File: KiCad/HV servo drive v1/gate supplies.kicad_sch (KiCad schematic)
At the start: 21 parts, among them U20 WRF0505S-3WR2, U21 B0505MT-1WR4, U8 B0505MT-1WR4

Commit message: KiCad 8.0 update
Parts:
- renumbered C105 to C101, C26 to C103, C44 to C104, C106 to C105, C103 to C106, C42 to C26, C104 to C42, C101 to C43, C43 to C44, L6 to L10, L10 to L6, TP5 to TP3, TP3 to TP5, U21 to U20, U8 to U21, U20 to U8

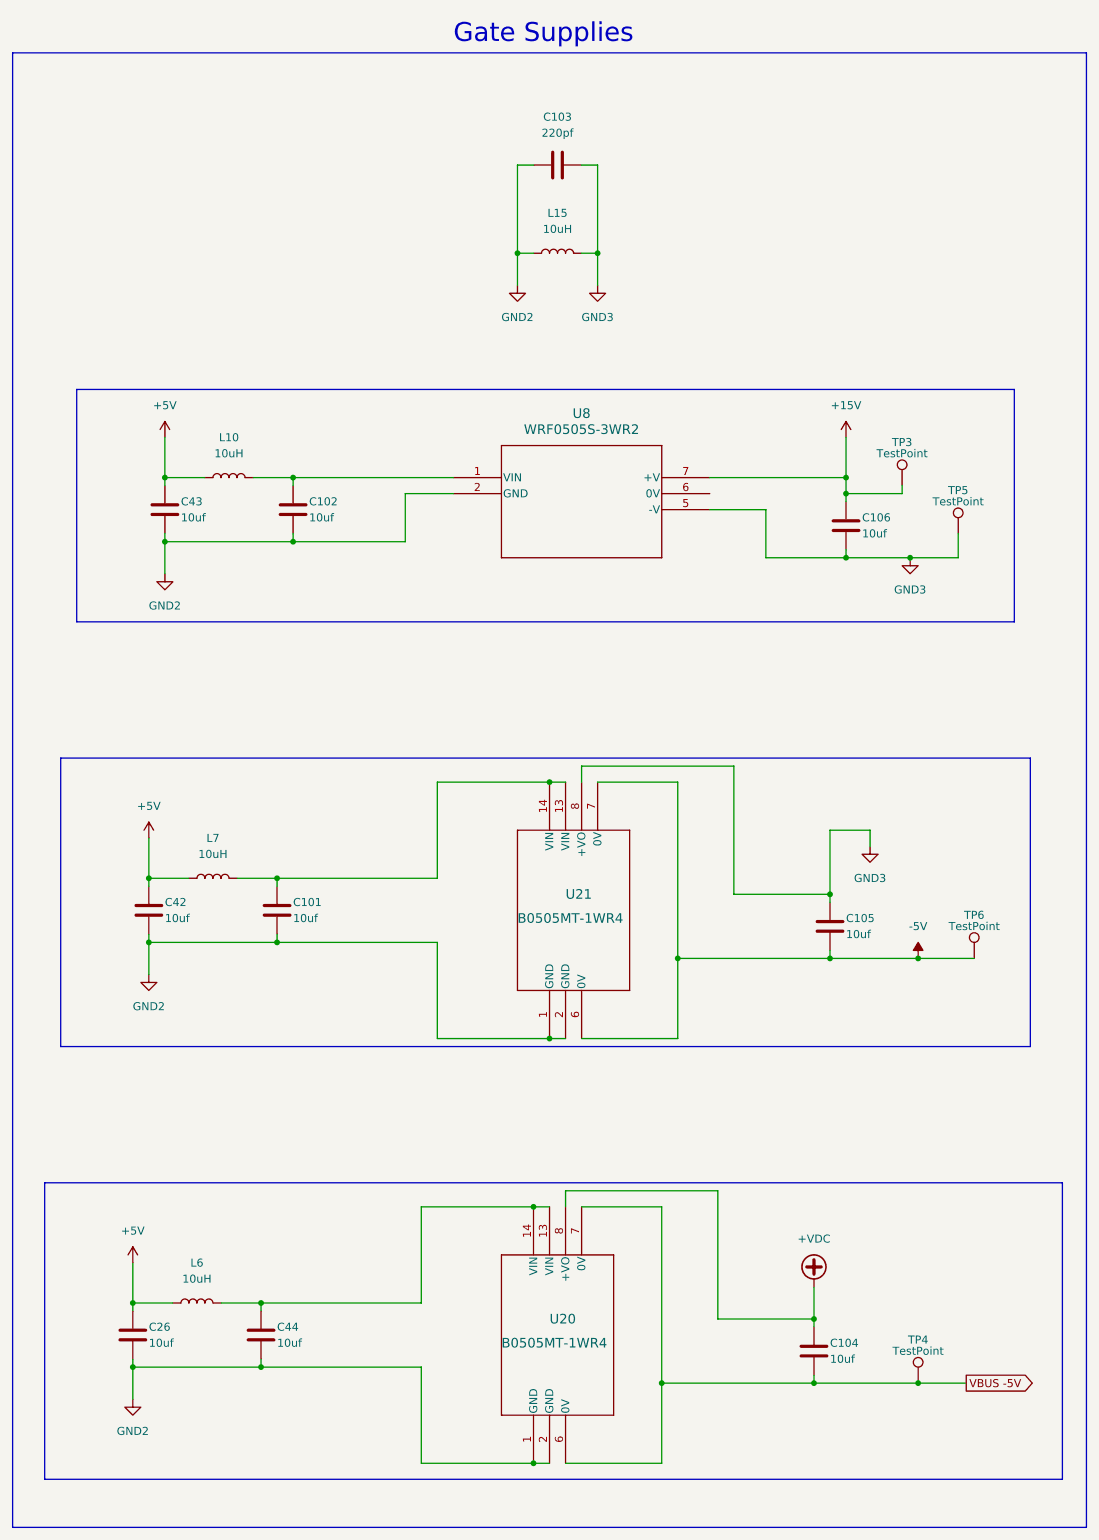
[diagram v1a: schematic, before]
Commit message: start rev 2 changes
fix component references, fix rj45 and dc-dc converter footprints, add RLC filters on all power connectors, add more mounting holes
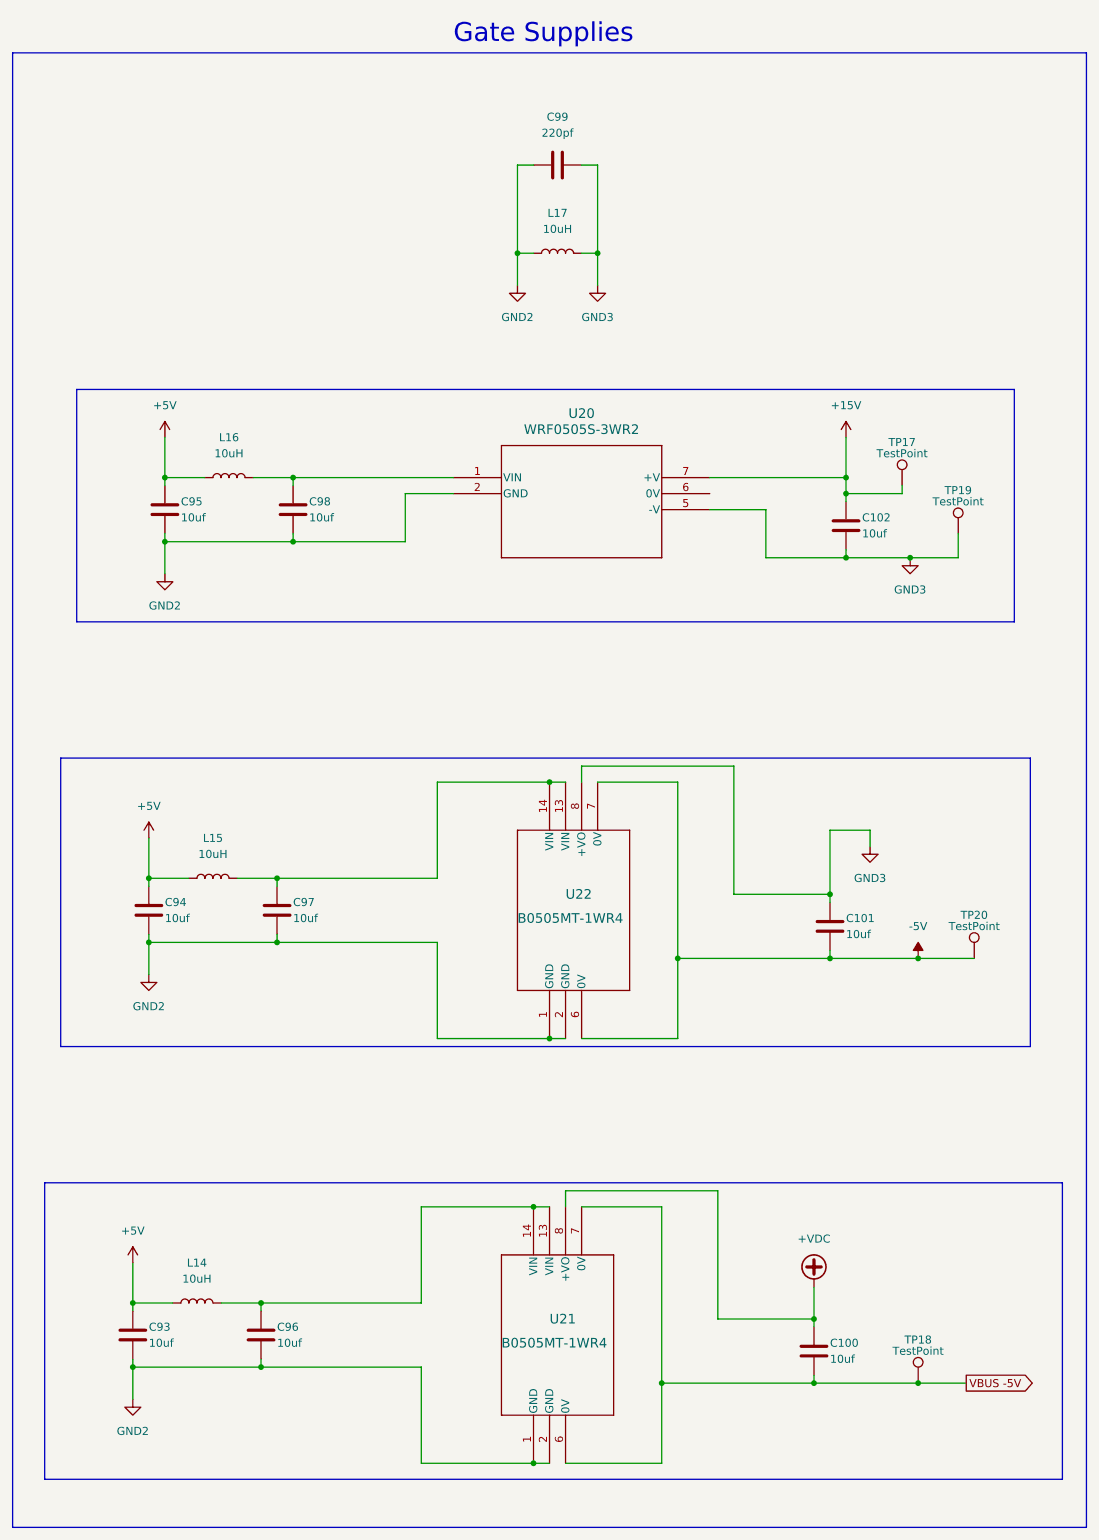
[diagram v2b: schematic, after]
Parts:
- U20: renamed from U8; footprint footprints:F0505S-2WR3 -> footprints:B0515
- renumbered C104 to C100, C105 to C101, C106 to C102, C26 to C93, C42 to C94, C43 to C95, C44 to C96, C101 to C97, C102 to C98, C103 to C99, L6 to L14, L7 to L15, L10 to L16, L15 to L17, TP3 to TP17, TP4 to TP18, TP5 to TP19, TP6 to TP20, U20 to U21, U21 to U22

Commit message: update to rev 2.1
basically the same version as in the FOC youtube video, with some minor issues fixed
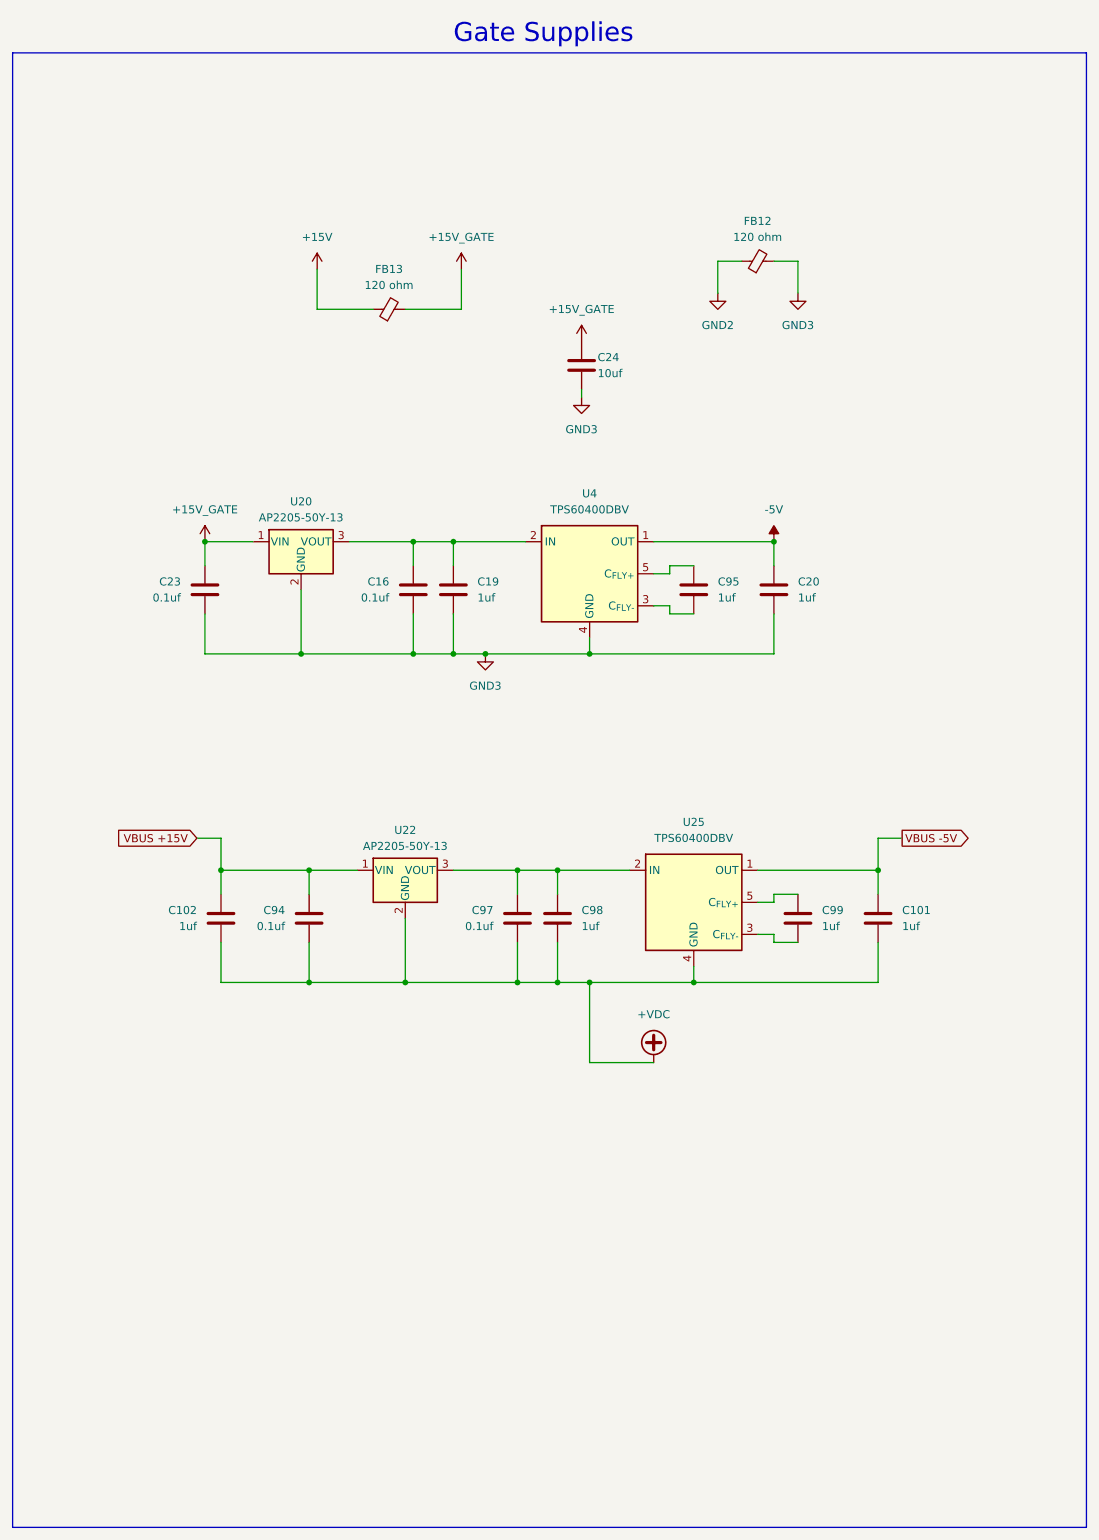
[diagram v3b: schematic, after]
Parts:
- removed C100, C93, C96: 10uf, Capacitor_SMD:C_0805_2012Metric, symbol Device:C
- removed L14, L15, L16, L17: 10uH, Inductor_SMD:L_1008_2520Metric, symbol Device:L
- removed TP17, TP18, TP19, TP20: TestPoint, footprints:TestPoint_Pad_3.1x1.6mm, symbol Connector:TestPoint
- removed U20: WRF0505S-3WR2, footprints:B0515, symbol F0505S DC-DC:F0505S
- removed U21, U22: B0505MT-1WR4, footprints:B05xxMT-1WR4_MNS, symbol B0505MT:B0505MT-1WR4
- added C16, C23: 0.1uf, Capacitor_SMD:C_0603_1608Metric, symbol Device:C
- added C19, C20: 1uf, Capacitor_SMD:C_0603_1608Metric, symbol Device:C
- added C24: 10uf, Capacitor_SMD:C_0805_2012Metric, symbol Device:C
- added FB12, FB13: 120 ohm, Inductor_SMD:L_0603_1608Metric, symbol Device:FerriteBead_Small
- added U20, U22: AP2205-50Y-13, Package_TO_SOT_SMD:SOT-89-3, symbol Regulator_Linear:AP2204R-5.0
- added U25, U4: TPS60400DBV, Package_TO_SOT_SMD:SOT-23-5, symbol Regulator_SwitchedCapacitor:TPS60400DBV
- C101, C102, C95, C98: value 10uf -> 1uf; footprint Capacitor_SMD:C_0805_2012Metric -> Capacitor_SMD:C_0603_1608Metric; Generic Allowed? (none) -> yes; Manufacturer (none) -> Samsung Electro-Mechanics; Part number (none) -> CL10A105KB8NNNC
- C94, C97: value 10uf -> 0.1uf; footprint Capacitor_SMD:C_0805_2012Metric -> Capacitor_SMD:C_0603_1608Metric; Generic Allowed? (none) -> yes; Manufacturer (none) -> YAGEO; Part number (none) -> CC0603ZRY5V9BB104
- C99: value 220pf -> 1uf; Generic Allowed? (none) -> yes; Manufacturer (none) -> Samsung Electro-Mechanics; Part number (none) -> CL10A105KB8NNNC
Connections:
- net +15V: now also FB13.1; no longer C102.1
- net +VDC: now also C101.2, C102.2, C94.2, C97.2, C98.2, U22.2 (GND), U25.4 (GND)
- net -5V: now also C20.1, U4.1 (OUT); no longer C101.2
- net GND2: now also FB12.1; no longer C94.2, C95.2, C97.2, C98.2, C99.2
- net GND3: now also C16.2, C19.2, C20.2, C23.2, C24.2, FB12.2, U20.2 (GND), U4.4 (GND); no longer C101.1, C102.2, C99.1
- net VBUS -5V: now also C101.1, U25.1 (OUT)
- net at C97.1: now also C98.1, U22.3 (VOUT), U25.2 (IN)
- net +5V: no longer names the net of C95.1
- net +5V: now also U4.5 (C_{FLY+}); no longer C94.1
- new net: C16.1, C19.1, U20.3 (VOUT), U4.2 (IN)
- new net: C95.2, U4.3 (C_{FLY-})
- new net: C99.1, U25.5 (C_{FLY+})
- new net: C99.2, U25.3 (C_{FLY-})
- new net +15V_GATE: C23.1, C24.1, FB13.2, U20.1 (VIN)
- new net VBUS +15V: C102.1, C94.1, U22.1 (VIN)
